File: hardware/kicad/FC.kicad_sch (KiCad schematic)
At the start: 8 parts, among them J1 xt30, U1 TPS7A4533DCQR

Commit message: work on pcb
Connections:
- net VBAT_DIRECT: now reaches F4.1, J1.2 (N)
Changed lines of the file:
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@@
     (effects (font (size 1 1)) (justify left bottom))
+  )
+  (label "VBAT_DIRECT" (at 135.255 147.32 0) (fields_autoplaced)
+    (effects (font (size 0.63 0.63)) (justify left bottom))
   )
   (label "MISO" (at 61.595 36.195 0) (fields_autoplaced)

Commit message: sync
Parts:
- removed D2: LSM115JE3, LSM115JE3:LSM115JE3, symbol Device:D
- added D7: CUS08F30,H3F, Diode_SMD:D_SOD-323_HandSoldering, symbol Device:D_Schottky
- D1: symbol Device:D -> Device:D_Schottky
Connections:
- net VBUS: now also D7.2 (A)
- net at C1.1, D1.1 (K), U1.1 (~{SHDN})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: now also D7.1 (K)
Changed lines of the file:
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@@
     (stroke (width 0) (type default))
-  )
-  (polyline (pts (xy 264.16 168.91) (xy 264.16 133.985))
-    (stroke (width 0) (type dash))
   )
   (wire (pts (xy 193.04 32.385) (xy 202.565 32.385))
@@
     (stroke (width 0) (type default))
   )
+  (polyline (pts (xy 264.795 135.89) (xy 264.795 170.18))
+    (stroke (width 0) (type dash))
+  )
   (wire (pts (xy 244.475 151.765) (xy 243.205 151.765))
     (stroke (width 0) (type default))
   )
+  (polyline (pts (xy 123.825 135.89) (xy 264.795 135.89))
+    (stroke (width 0) (type dash))
+  )
   (wire (pts (xy 189.865 147.32) (xy 208.915 147.32))
     (stroke (width 0) (type default))
@@
     (stroke (width 0) (type default))
   )
+  (polyline (pts (xy 123.825 135.89) (xy 123.825 170.18))
+    (stroke (width 0) (type dash))
+  )
   (bus (pts (xy 80.01 41.91) (xy 80.01 45.085))
     (stroke (width 0) (type default))
@@
     (stroke (width 0) (type default))
   )
-  (polyline (pts (xy 160.02 168.91) (xy 264.16 168.91))
-    (stroke (width 0) (type dash))
-  )
   (wire (pts (xy 244.475 147.32) (xy 250.825 147.32))
     (stroke (width 0) (type default))
@@
     (stroke (width 0) (type default))
   )
-  (polyline (pts (xy 264.16 133.985) (xy 160.02 133.985))
-    (stroke (width 0) (type dash))
-  )
   (wire (pts (xy 17.78 180.34) (xy 31.115 180.34))
     (stroke (width 0) (type default))
@@
   (wire (pts (xy 59.69 123.825) (xy 69.85 123.825))
     (stroke (width 0) (type default))
+  )
+  (polyline (pts (xy 264.795 170.18) (xy 123.825 170.18))
+    (stroke (width 0) (type dash))
   )
   (polyline (pts (xy 75.565 67.31) (xy 75.565 103.505))
@@
     (effects (font (size 2 2) (thickness 0.4) bold) (justify left bottom))
   )
-  (text "POWER" (at 160.02 133.35 0)
+  (text "POWER" (at 123.825 134.62 0)
     (effects (font (size 2 2) (thickness 0.4) bold) (justify left bottom))
   )
@@
     )
   )
+  (symbol (lib_name "D_Schottky_2") (lib_id "Device:D_Schottky") (at 189.865 153.035 270) (unit 1)
+    (in_bom yes) (on_board yes) (dnp no)
+    (property "Reference" "D7" (at 198.12 152.4 90)
+      (effects (font (size 1.27 1.27)))
+    )
+    (property "Value" "CUS08F30,H3F" (at 198.755 154.305 90)
+      (effects (font (size 1.27 1.27)))
+    )
+    (property "Footprint" "Diode_SMD:D_SOD-323_HandSoldering" (at 195.1482 153.4668 0)
+      (effects (font (size 1.27 1.27)) hide)
+    )
+    (property "Datasheet" "https://toshiba.semicon-storage.com/info/docget.jsp?did=9019&prodName=CUS08F30" (at 195.1482 153.4668 0)
+      (effects (font (size 1.27 1.27)) hide)
+    )
+    (property "Digikey" "https://www.digikey.com/en/products/detail/toshiba-semiconductor-and-storage/CUS08F30-H3F/5114298" (at 195.1482 153.4668 0)
+      (effects (font (size 1.27 1.27)) hide)
+    )
+    (pin "1")
+    (pin "2")
+    (instances
+      (project "FC"
+        (path "/54cce219-8b98-4e71-96c4-f9ee784aa3bc"
+          (reference "D7") (unit 1)
+        )
+      )
+      (project "altimeter-dev-board"
+        (path "/653cf154-8d56-4d90-88f3-bb1eb3f1f3f4/c8d1b71b-6ddd-47e2-85a2-5c4ab6b20140"
+          (reference "D2") (unit 1)
+        )
+      )
+    )
+  )
   (symbol (lib_id "power:GND") (at 153.67 158.115 0) (unit 1)
     (in_bom yes) (on_board yes) (dnp no) (fields_autoplaced)
@@
     )
   )
-  (symbol (lib_id "Device:D") (at 183.515 147.32 180) (unit 1)
+  (symbol (lib_name "D_Schottky_1") (lib_id "Device:D_Schottky") (at 183.515 147.32 180) (unit 1)
     (in_bom yes) (on_board yes) (dnp no)
     (property "Reference" "D1" (at 183.515 142.875 0)
@@
       (effects (font (size 1.27 1.27)) hide)
     )
-    (property "Datasheet" "https://mm.digikey.com/Volume0/opasdata/d220001/medias/docus/794/LSM115J.pdf" (at 183.515 147.32 0)
+    (property "Datasheet" "~" (at 183.515 147.32 0)
       (effects (font (size 1.27 1.27)) hide)
     )
@@
         )
       )
-    )
-  )
-  (symbol (lib_id "Device:D") (at 189.865 153.035 270) (unit 1)
-    (in_bom yes) (on_board yes) (dnp no)
-    (property "Reference" "D2" (at 193.04 151.13 90)
-      (effects (font (size 1.27 1.27)))
-    )
-    (property "Value" "LSM115JE3" (at 197.485 153.035 90)
-      (effects (font (size 1.27 1.27)))
-    )
-    (property "Footprint" "LSM115JE3:LSM115JE3" (at 189.865 153.035 0)
-      (effects (font (size 1.27 1.27)) hide)
-    )
-    (property "Datasheet" "https://mm.digikey.com/Volume0/opasdata/d220001/medias/docus/794/LSM115J.pdf" (at 189.865 153.035 0)
-      (effects (font (size 1.27 1.27)) hide)
-    )
-    (property "Sim.Device" "D" (at 189.865 153.035 0)
-      (effects (font (size 1.27 1.27)) hide)
-    )
-    (property "Sim.Pins" "1=K 2=A" (at 189.865 153.035 0)
-      (effects (font (size 1.27 1.27)) hide)
-    )
-    (property "Digikey" "https://www.digikey.com/en/products/detail/microchip-technology/LSM115JE3-TR13/1634473" (at 189.865 153.035 0)
-      (effects (font (size 1.27 1.27)) hide)
-    )
-    (pin "1")
-    (pin "2")
-    (instances
-      (project "FC"
-        (path "/54cce219-8b98-4e71-96c4-f9ee784aa3bc"
-          (reference "D2") (unit 1)
-        )
-      )

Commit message: power routing
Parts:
- D8: Digikey https://www.digikey.com/en/products/detail/vishay-general-semiconductor-diodes-division/V15PM153-M3-I/16683129 -> https://www.digikey.com/en/products/detail/vishay-general-semiconductor-diodes-division/V15PM153-M3-H/16683075
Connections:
- net VREG_IN: now reaches C1.1, D1.1 (K), D7.1 (K), U1.1 (~{SHDN}), U1.2 (IN)
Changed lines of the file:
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@@
+    (effects (font (size 1.27 1.27)) (justify left bottom))
+  )
+  (label "VREG_IN" (at 201.93 147.32 0) (fields_autoplaced)
     (effects (font (size 1.27 1.27)) (justify left bottom))
   )
@@
       (effects (font (size 1.27 1.27)) hide)
     )
-    (property "Digikey" "https://www.digikey.com/en/products/detail/vishay-general-semiconductor-diodes-division/V15PM153-M3-I/16683129" (at 163.83 154.305 0)
-      (effects (font (size 1.27 1.27)) hide)
-    )
+    (property "Digikey" "https://www.digikey.com/en/products/detail/vishay-general-semiconductor-diodes-division/V15PM153-M3-H/16683075" (at 163.83 154.305 0)
+      (effects (font (size 1.27 1.27)) hide)
+    )

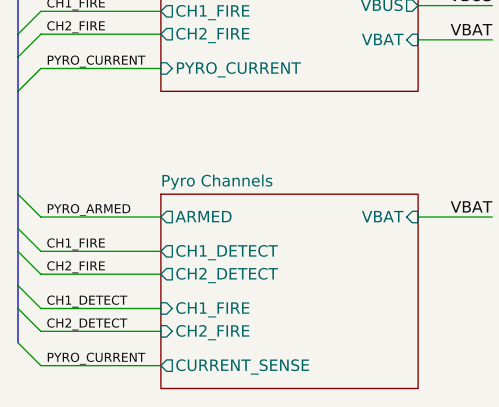
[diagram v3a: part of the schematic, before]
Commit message: massive routing progress
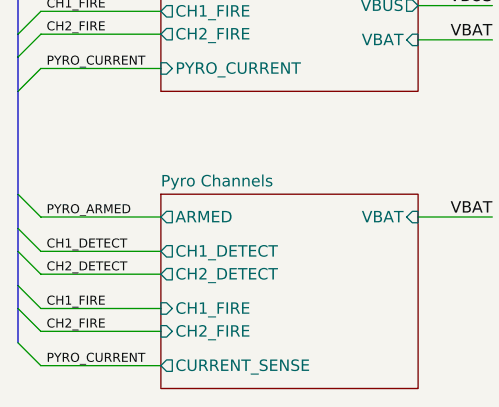
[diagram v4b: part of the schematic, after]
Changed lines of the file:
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@@
     (effects (font (size 1.27 1.27)) (justify left bottom))
   )
-  (label "CH1_DETECT" (at 18.415 180.34 0) (fields_autoplaced)
+  (label "CH1_DETECT" (at 18.415 173.99 0) (fields_autoplaced)
     (effects (font (size 1 1)) (justify left bottom))
   )
@@
     (effects (font (size 1.27 1.27)) (justify right bottom))
   )
-  (label "CH2_DETECT" (at 18.415 182.88 0) (fields_autoplaced)
+  (label "CH2_DETECT" (at 18.415 176.53 0) (fields_autoplaced)
     (effects (font (size 1 1)) (justify left bottom))
   )
-  (label "CH2_FIRE" (at 18.415 176.53 0) (fields_autoplaced)
+  (label "CH2_FIRE" (at 18.415 182.88 0) (fields_autoplaced)
     (effects (font (size 1 1)) (justify left bottom))
   )
@@
     (effects (font (size 1.27 1.27)) (justify right bottom))
   )
-  (label "CH1_FIRE" (at 18.415 173.99 0) (fields_autoplaced)
+  (label "CH1_FIRE" (at 18.415 180.34 0) (fields_autoplaced)
     (effects (font (size 1 1)) (justify left bottom))
   )

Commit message: sync
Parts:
- C1: Digikey (none) -> https://www.digikey.com/en/products/detail/cal-chip-electro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
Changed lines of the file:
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@@
       (effects (font (size 1.27 1.27)) hide)
     )
-    (property "Datasheet" "~" (at 208.915 152.4 0)
+    (property "Datasheet" "https://88ce57.p3cdn1.secureserver.net/wp-content/uploads/2023/01/gmc_series-2.pdf" (at 208.915 152.4 0)
       (effects (font (size 1.27 1.27)) hide)
     )
+    (property "Digikey" "https://www.digikey.com/en/products/detail/cal-chip-electronics-inc/GMC31X5R107M10NT/18151070" (at 208.915 152.4 0)
+      (effects (font (size 1.27 1.27)) hide)
+    )

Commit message: appended .off to old files
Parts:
- renumbered F4 to F2
